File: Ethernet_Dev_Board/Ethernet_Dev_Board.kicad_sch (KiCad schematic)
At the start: 27 parts, among them J101 Power In, J102 5V, J103 3.3V, J104 3.3VA, J105 3.3VD, U101 AZ1117

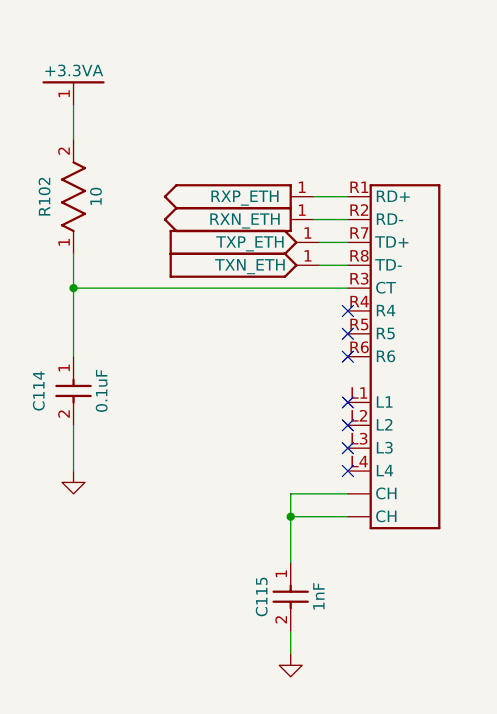
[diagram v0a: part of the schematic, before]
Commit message: Added info to another RJ45 connector
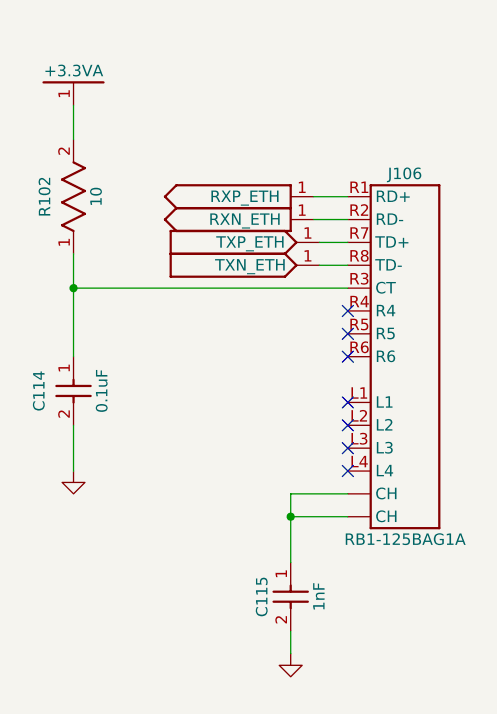
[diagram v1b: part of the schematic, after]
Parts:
- J106: Distributor (none) -> Digikey; Distributor PN (none) -> 1278-1011-ND; Mfg. (none) -> WIZnet; Mfg. PN (none) -> RB1-125BAG1A
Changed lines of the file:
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@@
 		(on_board yes)
 		(dnp no)
-		(fields_autoplaced yes)
 		(property "Reference" "J106"
-			(at 265.43 82.55 0)
+			(at 265.43 62.23 0)
 			(effects
 				(font
 					(size 1.27 1.27)
 				)
-				(hide yes)
 			)
 		)
@@
 			)
 		)
-		(property "Datasheet" ""
+		(property "Datasheet" "https://mm.digikey.com/Volume0/opasdata/d220001/medias/docus/11/RB1-125BAG1A_ApprovalSheet.pdf"
 			(at 265.43 82.55 0)
 			(effects
@@
 			(at 265.43 82.55 0)
 			(effects
+				(font
+					(size 1.27 1.27)
+				)
+				(hide yes)
+			)
+		)
+		(property "Mfg." "WIZnet"
+			(at 265.43 82.55 0)
+			(effects
+				(font
+					(size 1.27 1.27)
+				)
+				(hide yes)
+			)
+		)
+		(property "Mfg. PN" "RB1-125BAG1A"
+			(at 265.43 102.87 0)
+			(effects
+				(font
+					(size 1.27 1.27)
+				)
+			)
+		)
+		(property "Distributor" "Digikey"
+			(at 265.43 82.55 0)
+			(effects
+				(font
+					(size 1.27 1.27)
+				)
+				(hide yes)
+			)
+		)
+		(property "Distributor PN" "1278-1011-ND"
+			(at 265.43 82.55 0)
+			(effects
